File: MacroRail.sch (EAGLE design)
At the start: 19 parts, among them CN1 1X4-3.5MM, J1 SJ1-2503A, U1 ESP32DEVKITC, U2 TCM2209-V1.2

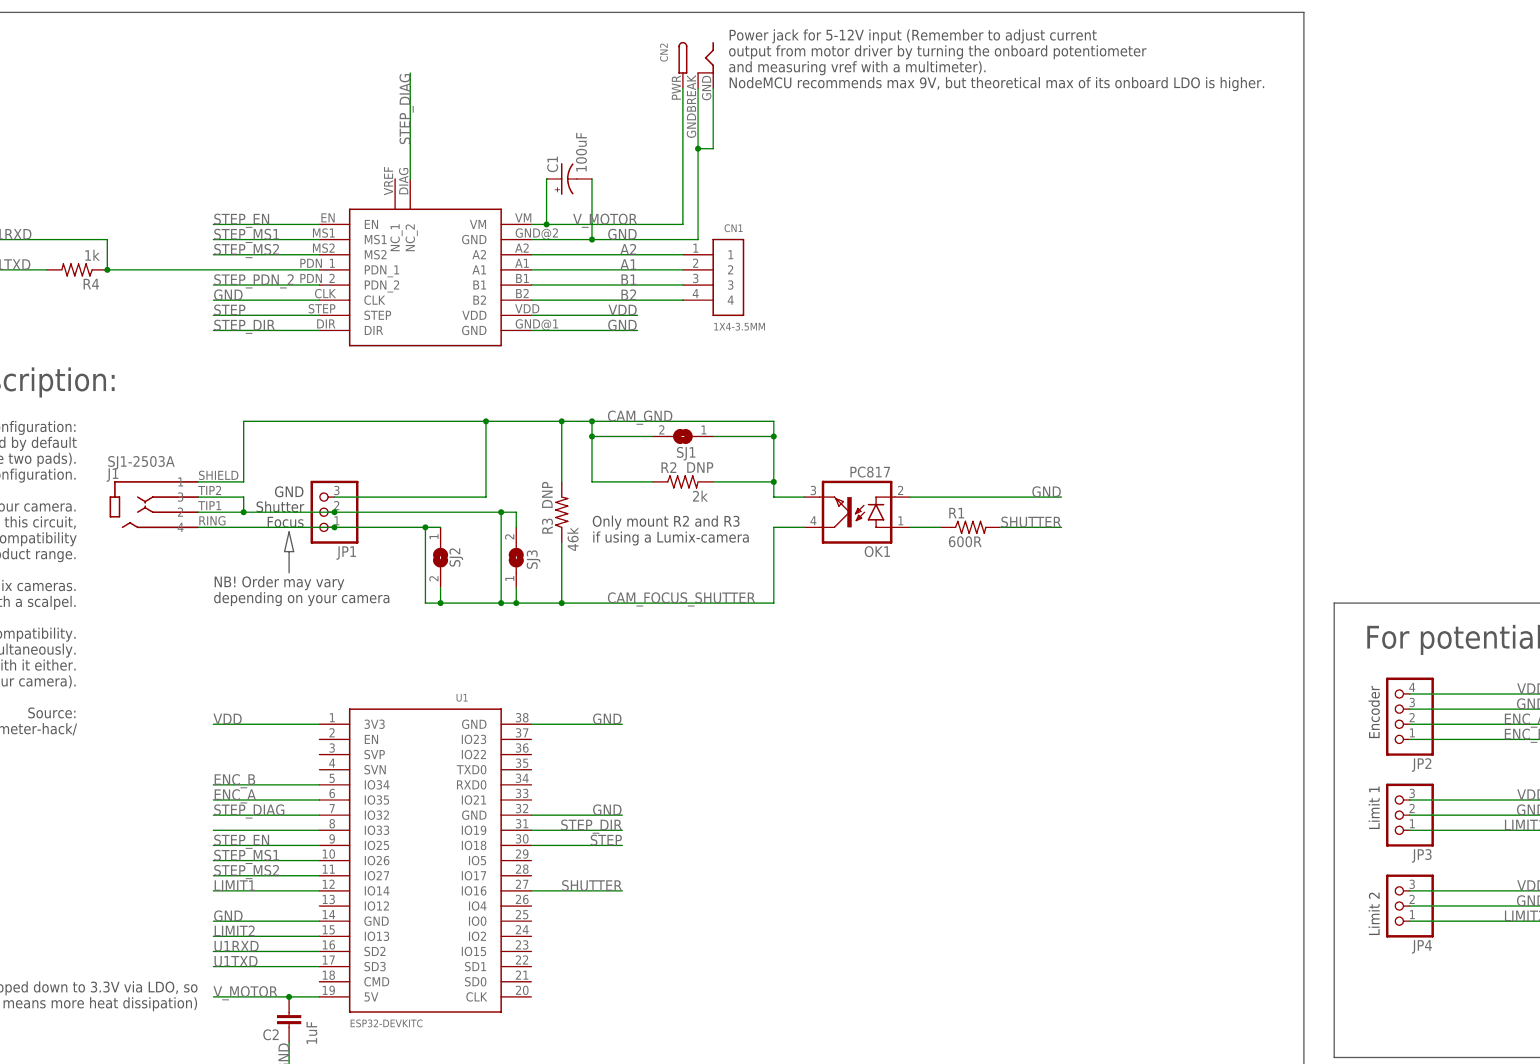
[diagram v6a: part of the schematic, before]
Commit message: V1.1
Add optional index pin and produce new output files
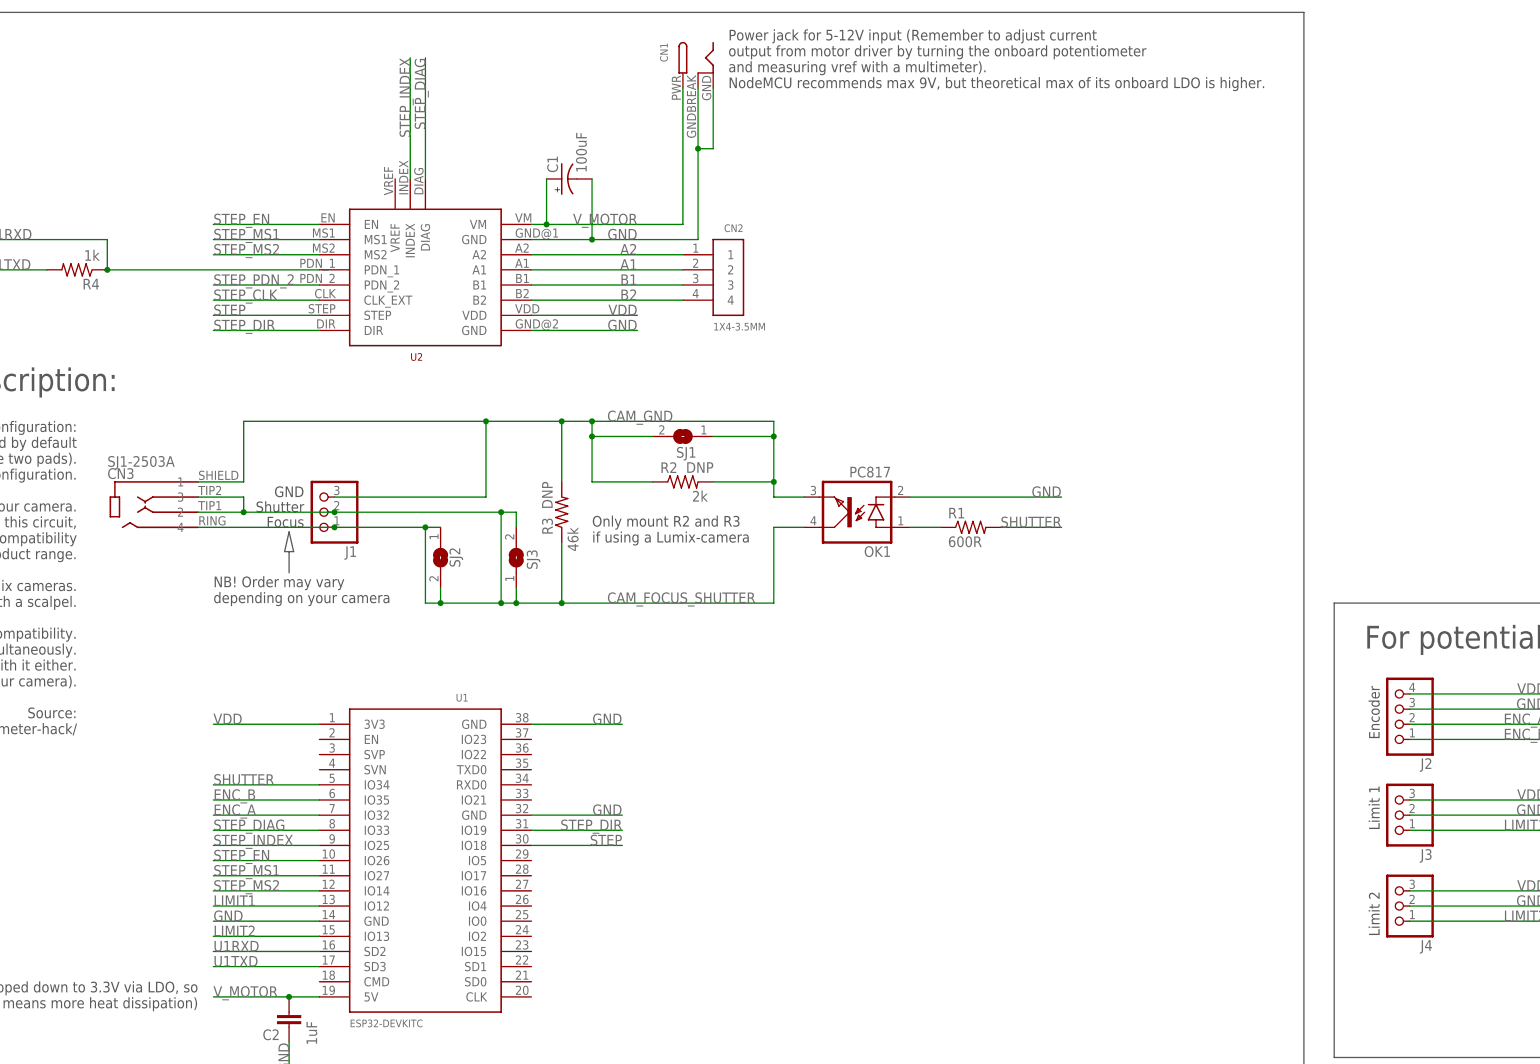
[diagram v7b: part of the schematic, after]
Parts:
- removed JP1: (no value), adafruit:PINHD-1X3CB
- added CN3: SJ1-2503A, 00-Random-Components-Simen:SJ1-2503A
- CN1: value 1X4-3.5MM -> (none); device adafruit:1X4-3.5MM -> adafruit:DCBARRELPTH
- CN2: value (none) -> 1X4-3.5MM; device adafruit:DCBARRELPTH -> adafruit:1X4-3.5MM
- J1: value SJ1-2503A -> (none); device 00-Random-Components-Simen:SJ1-2503A -> adafruit:PINHD-1X3CB
- U2: value TCM2209-V1.2 -> TMC2209-V1.2+INDEX; device 00-Random-Components-Simen:TCM2209-V1.2 -> 00-Random-Components-Simen:TMC2209-V1.2+INDEX
- renumbered JP2 to J2, JP3 to J3, JP4 to J4
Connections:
- removed net N$2: U1.IO33
- new net STEP_CLK: U2.CLK_EXT
- new net STEP_INDEX: U1.IO25, U2.INDEX
- net A1: now also CN2.2; no longer CN1.2
- net A2: now also CN2.1; no longer CN1.1
- net B1: now also CN2.3; no longer CN1.3
- net B2: now also CN2.4; no longer CN1.4
- net CAM_FOCUS_SHUTTER: now also CN3.2, CN3.3, CN3.4, J1.1; no longer J1.3, J1.4, JP1.1, JP1.2
- net CAM_GND: now also CN3.1, J1.3; no longer J1.1, JP1.3
- net ENC_A: now also U1.IO32; no longer U1.IO35
- net ENC_B: now also U1.IO35; no longer U1.IO34
- net GND: now also CN1.GND, CN1.GNDBREAK; no longer CN2.GND, CN2.GNDBREAK, U2.CLK
- net LIMIT1: now also U1.IO12; no longer U1.IO14
- net SHUTTER: now also U1.IO34; no longer U1.IO16
- net STEP_DIAG: now also U1.IO33, U2.DIAG; no longer U1.IO32, U2.NC_2
- net STEP_EN: now also U1.IO26; no longer U1.IO25
- net STEP_MS1: now also U1.IO27; no longer U1.IO26
- net STEP_MS2: now also U1.IO14; no longer U1.IO27
- net V_MOTOR: now also CN1.PWR; no longer CN2.PWR

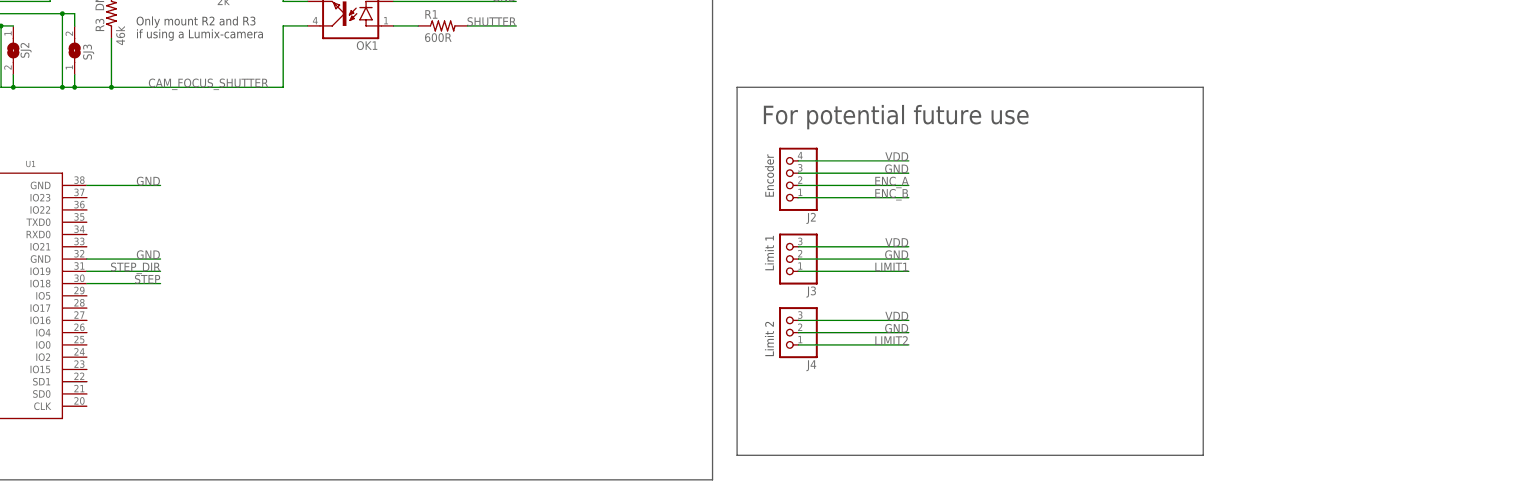
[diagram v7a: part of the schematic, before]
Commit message: Add possibility for driving high power LEDs
Since good illumination is important for macro photography, an option to drive high power LEDs via the Motorized Macro Rail PCB has been added.
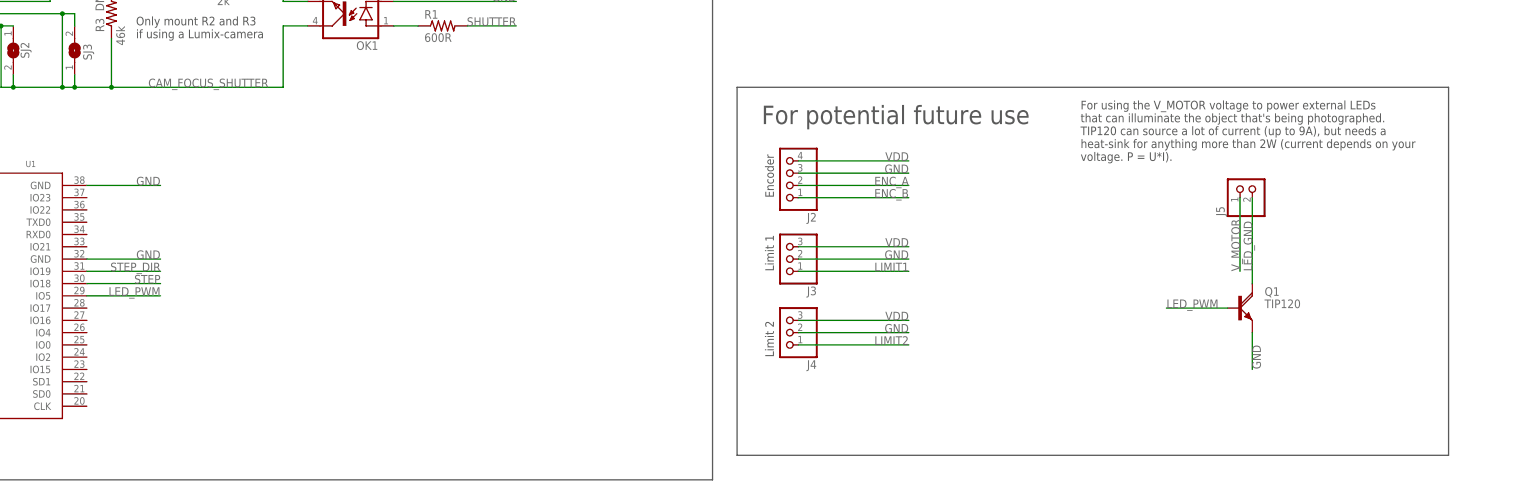
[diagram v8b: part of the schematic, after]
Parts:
- added J5: (no value), pinhead-custom:PINHD-1X2CLEAN
- added Q1: TIP120, 00-Random-Components-Simen:TIP120
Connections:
- new net LED_GND: J5.2, Q1.C
- new net LED_PWM: Q1.B, U1.IO5
- net GND: now also Q1.E
- net V_MOTOR: now also J5.1
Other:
- note added: "For using the V_MOTOR voltage to power external LEDs that can illuminate the object that's being photographed. TIP120 can source a lot of current (up to 9A), but needs a heat-sink for anything more than 2W (current depends on your voltage. P = U*I)."
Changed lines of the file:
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@@
 <part name="C2" library="rcl" library_urn="urn:adsk.eagle:library:334" deviceset="C-EU" device="050-024X044" package3d_urn="urn:adsk.eagle:package:23643/1" override_package3d_urn="urn:adsk.eagle:package:34322317/2" override_package_urn="urn:adsk.eagle:footprint:23147/1" value="1uF"/>
 <part name="R4" library="rcl" library_urn="urn:adsk.eagle:library:334" deviceset="R-US_" device="0207/7" package3d_urn="urn:adsk.eagle:package:23493/2" value="1k"/>
+<part name="Q1" library="00-Random-Components-Simen" library_urn="urn:adsk.eagle:library:24319138" deviceset="TIP120" device="" package3d_urn="urn:adsk.eagle:package:34683657/2" override_package3d_urn="urn:adsk.eagle:package:34684429/2" override_package_urn="urn:adsk.eagle:footprint:34683656/2"/>
+<part name="J5" library="pinhead-custom" library_urn="urn:adsk.eagle:library:7941324" deviceset="PINHD-1X2" device="CLEAN" override_package3d_urn="urn:adsk.eagle:package:34684443/2" override_package_urn="urn:adsk.eagle:footprint:34684444/1"/>
 </parts>
 <sheets>
@@
 <text x="162.56" y="55.88" size="1.778" layer="97" rot="R90">Encoder</text>
 <wire x1="154.94" y1="78.74" x2="154.94" y2="2.54" width="0.1524" layer="97"/>
-<wire x1="154.94" y1="2.54" x2="251.46" y2="2.54" width="0.1524" layer="97"/>
-<wire x1="251.46" y1="2.54" x2="251.46" y2="78.74" width="0.1524" layer="97"/>
-<wire x1="251.46" y1="78.74" x2="154.94" y2="78.74" width="0.1524" layer="97"/>
+<wire x1="154.94" y1="2.54" x2="302.26" y2="2.54" width="0.1524" layer="97"/>
+<wire x1="302.26" y1="2.54" x2="302.26" y2="78.74" width="0.1524" layer="97"/>
+<wire x1="302.26" y1="78.74" x2="154.94" y2="78.74" width="0.1524" layer="97"/>
 <text x="160.02" y="71.12" size="3.81" layer="97">For potential future use</text>
 <text x="-152.4" y="170.18" size="3.81" layer="97">Main functionality</text>
@@
 <text x="30.48" y="88.9" size="1.778" layer="97">Only mount R2 and R3
 if using a Lumix-camera</text>
+<text x="226.06" y="63.5" size="1.778" layer="97">For using the V_MOTOR voltage to power external LEDs
+that can illuminate the object that's being photographed.
+TIP120 can source a lot of current (up to 9A), but needs a
+heat-sink for anything more than 2W (current depends on your
+voltage. P = U*I).</text>
 </plain>
 <instances>
@@
 <attribute name="NAME" x="-52.07" y="133.1214" size="1.778" layer="95" rot="R180"/>
 <attribute name="VALUE" x="-52.07" y="137.922" size="1.778" layer="96" rot="R180"/>
+</instance>
+<instance part="Q1" gate="1" x="259.08" y="33.02" smashed="yes">
+<attribute name="NAME" x="264.16" y="35.56" size="1.778" layer="95"/>
+<attribute name="VALUE" x="264.16" y="33.02" size="1.778" layer="96"/>
+</instance>
+<instance part="J5" gate="G$1" x="261.62" y="58.42" smashed="yes" rot="R90">
+<attribute name="NAME" x="255.905" y="52.07" size="1.778" layer="95" rot="R90"/>
+<attribute name="VALUE" x="266.7" y="52.07" size="1.778" layer="96" rot="R90"/>
 </instance>
 </instances>
@@
 <junction x="-20.32" y="12.7"/>
 </segment>
+<segment>
+<pinref part="J5" gate="G$1" pin="1"/>
+<wire x1="259.08" y1="55.88" x2="259.08" y2="40.64" width="0.1524" layer="91"/>
+<label x="259.08" y="40.64" size="1.778" layer="95" rot="R90"/>
+</segment>
 </net>
 <net name="GND" class="1">
@@
 <label x="-20.32" y="0" size="1.778" layer="95" rot="R90"/>
 </segment>
+<segment>
+<pinref part="Q1" gate="1" pin="E"/>
+<wire x1="261.62" y1="27.94" x2="261.62" y2="20.32" width="0.1524" layer="91"/>
+<label x="261.62" y="25.4" size="1.778" layer="95" rot="R270"/>
+</segment>
 </net>
 <net name="A2" class="1">
@@
 </segment>
 </net>
+<net name="LED_PWM" class="0">
+<segment>
+<pinref part="Q1" gate="1" pin="B"/>
+<wire x1="256.54" y1="33.02" x2="243.84" y2="33.02" width="0.1524" layer="91"/>
+<label x="243.84" y="33.02" size="1.778" layer="95"/>
+</segment>
+<segment>
+<label x="35.56" y="35.56" size="1.778" layer="95" align="bottom-right"/>
+<pinref part="U1" gate="G$1" pin="IO5"/>
+<wire x1="20.32" y1="35.56" x2="35.56" y2="35.56" width="0.1524" layer="91"/>
+</segment>
+</net>
+<net name="LED_GND" class="0">
+<segment>
+<pinref part="Q1" gate="1" pin="C"/>
+<pinref part="J5" gate="G$1" pin="2"/>
+<wire x1="261.62" y1="38.1" x2="261.62" y2="55.88" width="0.1524" layer="91"/>
+<label x="261.62" y="40.64" size="1.778" layer="95" rot="R90"/>
+</segment>
+</net>
